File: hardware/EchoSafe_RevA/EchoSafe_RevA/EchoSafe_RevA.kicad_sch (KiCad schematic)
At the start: 27 parts, among them J1 TP4056_Module, J2 Conn_Harness_09, J3 Conn_Harness_09, J4 Conn_Harness_07, J5 Conn_Harness_07, U1 ESP32-S3-WROOM-1-N16R8, U2 MAX98357AETE+T, U3 DRV2605LDGS, U5 TCA9548A, U6 DRV2605LDGS, U7 DRV2605LDGS, U8 DRV2605LDGS

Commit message: Fix JST-SH footprint naming error, verify TP4056 pin spacing
Resolved both gaps flagged at the end of the footprint pass:

- JST-SH harness connector names were an unverified guess using a
  "BM0xB-SRSS-TB" prefix. Fetched the actual files from KiCad's own
  kicad-footprints repo and confirmed the real prefix is "SM0xB-SRSS-TB"
  -- JST_SH_SM09B-SRSS-TB_1x09-1MP_P1.00mm_Horizontal (9 signal + 2
  mounting pads) and JST_SH_SM07B-SRSS-TB_1x07-1MP_P1.00mm_Horizontal
  (7 signal + 2 mounting pads) both verified to exist with correct pad
  counts. Fixed all 8 occurrences across all 5 projects (J2/J3/J4/J5 in
  the central pod, one J1 per module).

- Checked TP4056 module pin spacing against multiple independent
  sources; 2.54mm/0.1" through-hole pitch is standard across common
  module variants, confirming the PinHeader_1x04_P2.54mm_Vertical
  placeholder already assigned. Noted this should still get a quick
  physical check against the actual board, since "HiLetGo TP4056"
  covers slightly different revisions.

Verified across all 5 files: paren balance intact, unique UUIDs.

Co-Authored-By: Claude Sonnet 5 <noreply@anthropic.com>
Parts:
- J2, J3: footprint Connector_JST:JST_SH_BM09B-SRSS-TB_1x09-1MP_P1.00mm_Horizontal -> Connector_JST:JST_SH_SM09B-SRSS-TB_1x09-1MP_P1.00mm_Horizontal
- J4, J5: footprint Connector_JST:JST_SH_BM07B-SRSS-TB_1x07-1MP_P1.00mm_Horizontal -> Connector_JST:JST_SH_SM07B-SRSS-TB_1x07-1MP_P1.00mm_Horizontal
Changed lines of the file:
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@@
 			(effects (font (size 1.27 1.27)) (justify left))
 		)
-		(property "Footprint" "Connector_JST:JST_SH_BM09B-SRSS-TB_1x09-1MP_P1.00mm_Horizontal"
+		(property "Footprint" "Connector_JST:JST_SH_SM09B-SRSS-TB_1x09-1MP_P1.00mm_Horizontal"
 			(at 30 195 0)
 			(effects (font (size 1.27 1.27) (italic yes)) (hide yes))
@@
 			(effects (font (size 1.27 1.27)) (justify left))
 		)
-		(property "Footprint" "Connector_JST:JST_SH_BM09B-SRSS-TB_1x09-1MP_P1.00mm_Horizontal"
+		(property "Footprint" "Connector_JST:JST_SH_SM09B-SRSS-TB_1x09-1MP_P1.00mm_Horizontal"
 			(at 70 195 0)
 			(effects (font (size 1.27 1.27) (italic yes)) (hide yes))
@@
 			(effects (font (size 1.27 1.27)) (justify left))
 		)
-		(property "Footprint" "Connector_JST:JST_SH_BM07B-SRSS-TB_1x07-1MP_P1.00mm_Horizontal"
+		(property "Footprint" "Connector_JST:JST_SH_SM07B-SRSS-TB_1x07-1MP_P1.00mm_Horizontal"
 			(at 110 195 0)
 			(effects (font (size 1.27 1.27) (italic yes)) (hide yes))
@@
 			(effects (font (size 1.27 1.27)) (justify left))
 		)
-		(property "Footprint" "Connector_JST:JST_SH_BM07B-SRSS-TB_1x07-1MP_P1.00mm_Horizontal"
+		(property "Footprint" "Connector_JST:JST_SH_SM07B-SRSS-TB_1x07-1MP_P1.00mm_Horizontal"
 			(at 250 195 0)
 			(effects (font (size 1.27 1.27) (italic yes)) (hide yes))

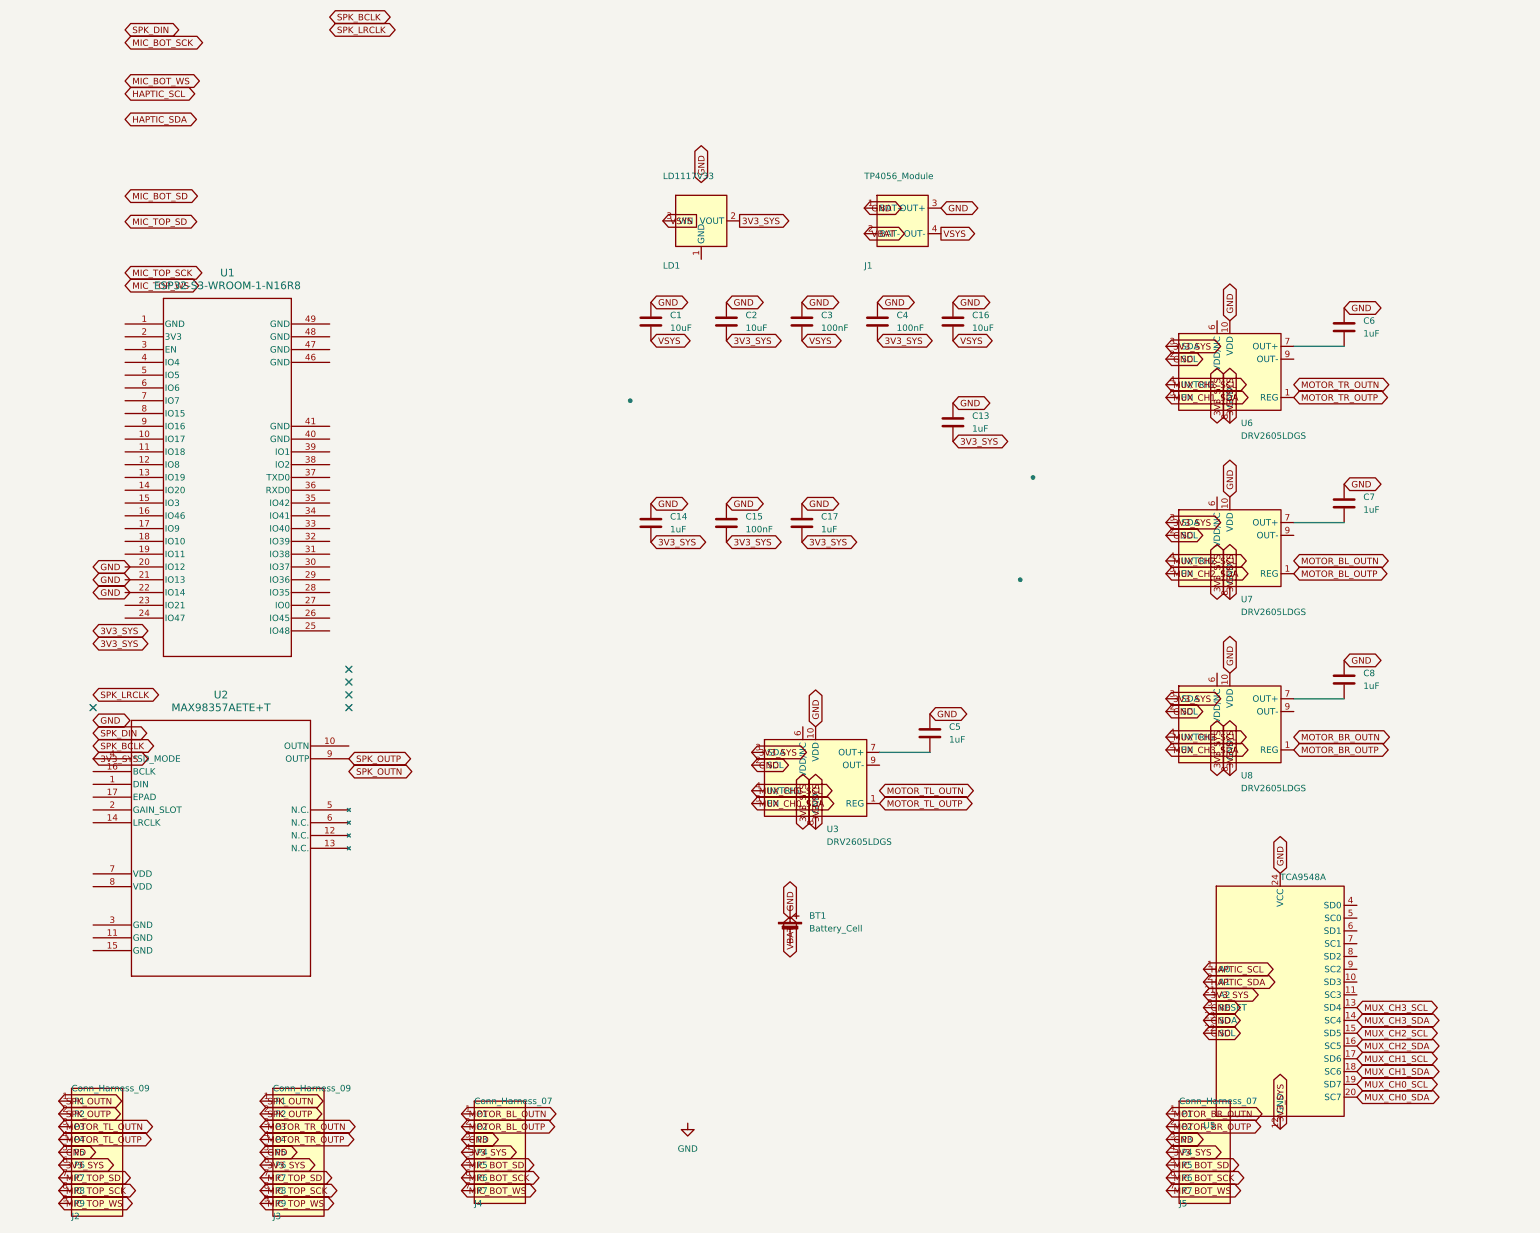
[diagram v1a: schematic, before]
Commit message: Fix session-wide Y-axis coordinate bug, power the ESP32 module
Discovered KiCad is actually installed on this machine and ran real
kicad-cli sch erc against every schematic for the first time, instead of
continuing to rely on text-based invariant checks alone. This surfaced a
fundamental bug affecting every schematic edit made this session:

Every label/wire/no-connect placed with a nonzero local Y pin offset used
placement_y + local_y instead of the correct placement_y - local_y --
KiCad symbol graphics are authored Y-up, the sheet is Y-down, and that
flip applies even at angle=0/no-mirror. The two formulas only agree when
local_y=0, which is why isolated spot-checks earlier in the session
happened to look right.

Fixed via a from-scratch single-pass correction (not sequential in-place
edits -- an earlier attempt at that approach introduced a second bug,
caught before committing: correcting one label could make its new
position collide with a not-yet-corrected label's old position, causing
a later step to move the wrong element). Final approach computes every
correction from an unmodified snapshot and applies them all in one pass
from a fixed baseline.

Verified by ERC before/after, not by the tooling that produced the bug:
- All 4 module projects: 21/21/17/17 raw violations -> 9/9/8/8, all
  expected (spare GPIOs, the already-documented placeholder-connector
  warning, and cross-project "power not driven" since the driving
  component lives in a different project's file).
- Central pod: down to 0 dangling labels, 0 genuinely unconnected pins.
  Remaining ~200 ERC items are exclusively pairwise power-rail type-
  mismatch warnings (expected on any board with this many ICs sharing
  3V3_SYS/GND), cosmetic off-grid warnings, and spare pins.

Also fixed, a genuine gap this same ERC pass surfaced (unrelated to the
Y-axis bug): the ESP32 module's own 3V3/GND/EN pins were never wired to
anything -- every peripheral got connected this session, the MCU's own
supply pins we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
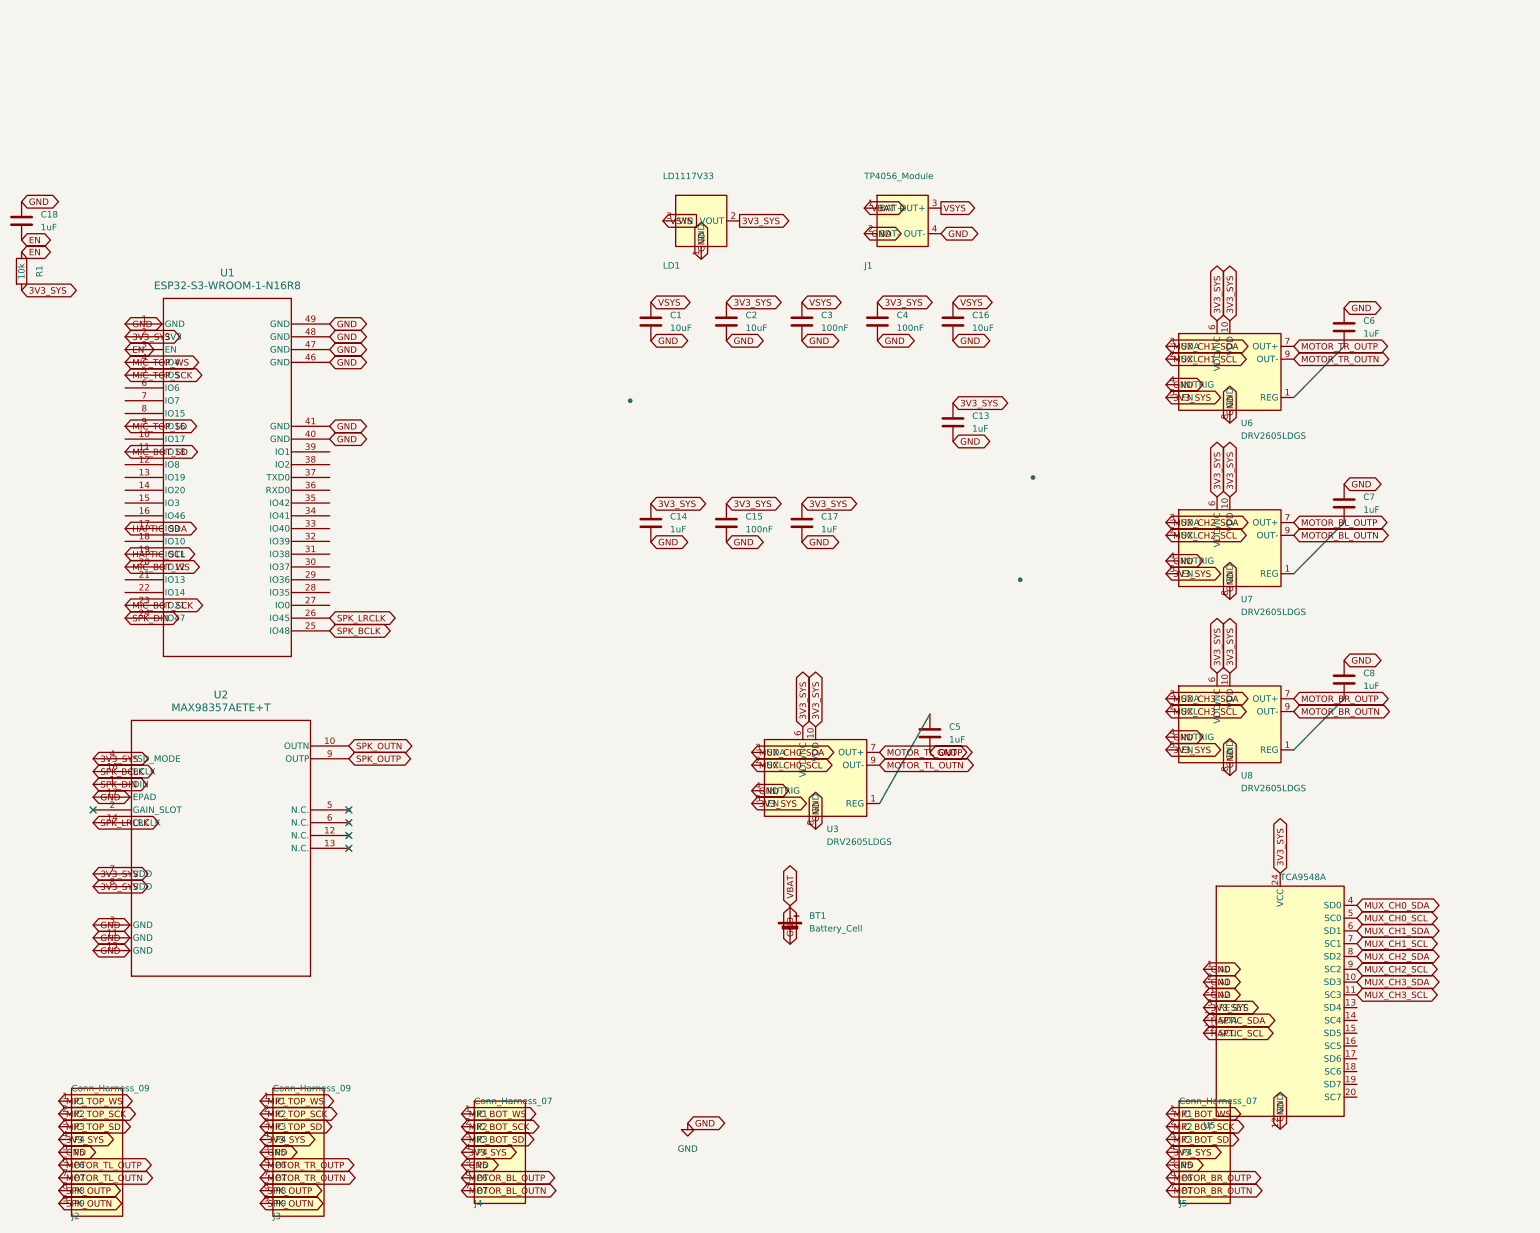
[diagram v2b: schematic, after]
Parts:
- added C18: 1uF, Capacitor_SMD:C_0603_1608Metric, symbol Device:C
- added R1: 10k, Resistor_SMD:R_0603_1608Metric, symbol Device:R
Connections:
- net 3V3_SYS: now also C13.1, C14.1, C15.1, C17.1, C2.1, C4.1, J2.4 (P4), J3.4 (P4), U1.2 (3V3), U2.7 (VDD), U2.8 (VDD), U3.10 (VDD), U3.5 (EN), U3.6 (VDD/NC), U5.24 (VCC), U5.3 (RESET), U6.10 (VDD), U6.5 (EN), U6.6 (VDD/NC), U7.10 (VDD), U7.5 (EN), U7.6 (VDD/NC), U8.10 (VDD), U8.5 (EN), U8.6 (VDD/NC), R1.2; no longer C13.2, C14.2, C15.2, C17.2, C2.2, C4.2, J2.6 (P6), J3.6 (P6), U3.3 (SDA), U3.8 (GND), U5.12 (GND), U5.21 (A2), U6.3 (SDA), U6.8 (GND), U7.3 (SDA), U7.8 (GND), U8.3 (SDA), U8.8 (GND)
- net GND: now also BT1.2 (-), C1.2, C13.2, C14.2, C15.2, C16.2, C17.2, C2.2, C3.2, C4.2, C5.2, J1.2 (BAT-), J1.4 (OUT-), J4.5 (P5), J5.5 (P5), LD1.1 (GND), U1.1 (GND), U1.40 (GND), U1.41 (GND), U1.46 (GND), U1.47 (GND), U1.48 (GND), U1.49 (GND), U2.11 (GND), U2.15 (GND), U2.17 (EPAD), U2.3 (GND), U3.4 (IN/TRIG), U3.8 (GND), U5.1 (A0), U5.12 (GND), U5.2 (A1), U5.21 (A2), U6.4 (IN/TRIG), U6.8 (GND), U7.4 (IN/TRIG), U7.8 (GND), U8.4 (IN/TRIG), U8.8 (GND), C18.1; no longer C1.1, C13.1, C14.1, C15.1, C16.1, C17.1, C2.1, C3.1, C4.1, C5.1, J1.1 (BAT+), J1.3 (OUT+), J4.3 (P3), J5.3 (P3), U3.10 (VDD), U3.2 (SCL), U5.22 (SCL), U5.23 (SDA), U5.24 (VCC), U5.3 (RESET), U6.10 (VDD), U6.2 (SCL), U7.10 (VDD), U7.2 (SCL), U8.10 (VDD), U8.2 (SCL)
- net HAPTIC_SCL: now also U1.19 (IO11), U5.22 (SCL); no longer U5.1 (A0)
- net HAPTIC_SDA: now also U1.17 (IO9), U5.23 (SDA); no longer U5.2 (A1)
- net MIC_BOT_SCK: now also J4.2 (P2), J5.2 (P2), U1.23 (IO21); no longer J4.6 (P6), J5.6 (P6)
- net MIC_BOT_SD: now also J4.3 (P3), J5.3 (P3), U1.11 (IO18); no longer J4.5 (P5), J5.5 (P5)
- net MIC_BOT_WS: now also J4.1 (P1), J5.1 (P1), U1.20 (IO12); no longer J4.7 (P7), J5.7 (P7)
- net MIC_TOP_SCK: now also J2.2 (P2), J3.2 (P2), U1.5 (IO5); no longer J2.8 (P8), J3.8 (P8)
- net MIC_TOP_SD: now also J2.3 (P3), J3.3 (P3), U1.9 (IO16); no longer J2.7 (P7), J3.7 (P7)
- net MIC_TOP_WS: now also J2.1 (P1), J3.1 (P1), U1.4 (IO4); no longer J2.9 (P9), J3.9 (P9)
- net MOTOR_BL_OUTN: now also J4.7 (P7), U7.9 (OUT-); no longer J4.1 (P1)
- net MOTOR_BL_OUTP: now also J4.6 (P6), U7.7 (OUT+); no longer J4.2 (P2), U7.1 (REG)
- net MOTOR_BR_OUTN: now also J5.7 (P7), U8.9 (OUT-); no longer J5.1 (P1)
- net MOTOR_BR_OUTP: now also J5.6 (P6), U8.7 (OUT+); no longer J5.2 (P2), U8.1 (REG)
- net MOTOR_TL_OUTN: now also J2.7 (P7), U3.9 (OUT-); no longer J2.3 (P3)
- net MOTOR_TL_OUTP: now also J2.6 (P6), U3.7 (OUT+); no longer J2.4 (P4), U3.1 (REG)
- net MOTOR_TR_OUTN: now also J3.7 (P7), U6.9 (OUT-); no longer J3.3 (P3)
- net MOTOR_TR_OUTP: now also J3.6 (P6), U6.7 (OUT+); no longer J3.4 (P4), U6.1 (REG)
- net MUX_CH0_SCL: now also U3.2 (SCL), U5.5 (SC0); no longer U3.4 (IN/TRIG), U5.19 (SD7)
- net MUX_CH0_SDA: now also U3.3 (SDA), U5.4 (SD0); no longer U3.5 (EN), U5.20 (SC7)
- net MUX_CH1_SCL: now also U5.7 (SC1), U6.2 (SCL); no longer U5.17 (SD6), U6.4 (IN/TRIG)
- net MUX_CH1_SDA: now also U5.6 (SD1), U6.3 (SDA); no longer U5.18 (SC6), U6.5 (EN)
- net MUX_CH2_SCL: now also U5.9 (SC2), U7.2 (SCL); no longer U5.15 (SD5), U7.4 (IN/TRIG)
- net MUX_CH2_SDA: now also U5.8 (SD2), U7.3 (SDA); no longer U5.16 (SC5), U7.5 (EN)
- net MUX_CH3_SCL: now also U5.11 (SC3), U8.2 (SCL); no longer U5.13 (SD4), U8.4 (IN/TRIG)
- net MUX_CH3_SDA: now also U5.10 (SD3), U8.3 (SDA); no longer U5.14 (SC4), U8.5 (EN)
- net SPK_BCLK: now also U1.25 (IO48), U2.16 (BCLK)
- net SPK_DIN: now also U1.24 (IO47), U2.1 (DIN)
- net SPK_LRCLK: now also U1.26 (IO45), U2.14 (LRCLK)
- net SPK_OUTN: now also J2.9 (P9), J3.9 (P9), U2.10 (OUTN); no longer J2.1 (P1), J3.1 (P1)
- net SPK_OUTP: now also J2.8 (P8), J3.8 (P8); no longer J2.2 (P2), J3.2 (P2)
- net VBAT: now also BT1.1 (+), J1.1 (BAT+); no longer J1.2 (BAT-)
- net VSYS: now also C1.1, C16.1, C3.1, J1.3 (OUT+); no longer C1.2, C16.2, C3.2, J1.4 (OUT-)
- net at C8.2: now also U8.1 (REG); no longer U8.7 (OUT+)
- net at C6.2: now also U6.1 (REG); no longer U6.7 (OUT+)
- net at C7.2: now also U7.1 (REG); no longer U7.7 (OUT+)
- net EN: now reaches U1.3 (EN)
- net EN: now also C18.2, R1.1
- new net: C5.1, U3.1 (REG)

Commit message: Complete PCB layout for all 5 boards, all DRC-clean
All 4 earpiece module boards and the central pod are now placed, fully
routed, and verified at 0 DRC violations / 0 unconnected pads via
kicad-cli. The central pod (the largest/densest board) was routed with
FreeRouting (Specctra DSN export/import) after hand-scripted routing
failed to converge; the last few gaps FreeRouting left were fixed by
hand with precise pad/via clearance geometry. Documented the full
approach and key lessons in CLAUDE.md for future reference.

Co-Authored-By: Claude Sonnet 5 <noreply@anthropic.com>
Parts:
- BT1: footprint Connector_JST:JST_PH_S2B_PH_K_1x02_P2.00mm_Horizontal -> Connector_JST:JST_PH_S2B-PH-K_1x02_P2.00mm_Horizontal
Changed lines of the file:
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@@
 			)
 		)
-		(property "Footprint" "Connector_JST:JST_PH_S2B_PH_K_1x02_P2.00mm_Horizontal"
+		(property "Footprint" "Connector_JST:JST_PH_S2B-PH-K_1x02_P2.00mm_Horizontal"
 			(at 167.64 149.606 90)
 			(effects

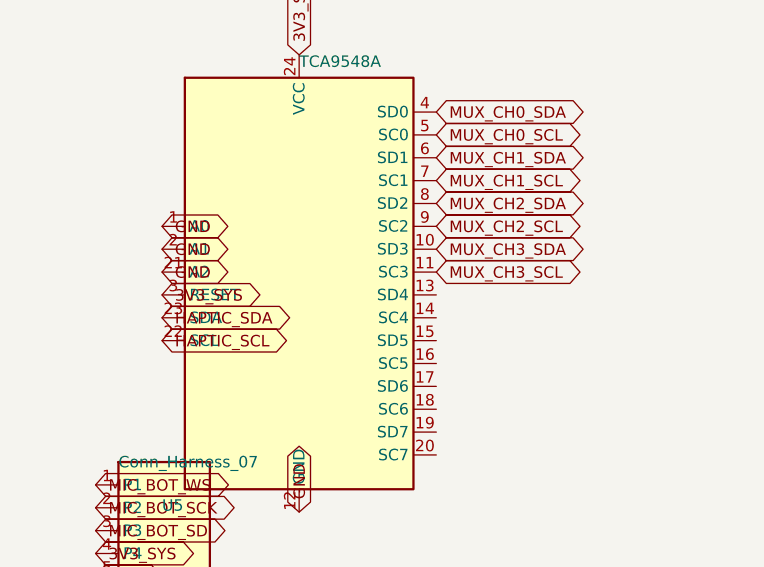
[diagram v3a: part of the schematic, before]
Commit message: Replace TCA9548A RESET direct tie with proper pull-up resistor
TI's TCA9548A datasheet specifies RESET should connect to VCC through
a pull-up resistor when unused, not a direct tie. Added R2 (10kΩ,
matching R1's EN pull-up convention) between RESET and 3V3_SYS.
Verified with kicad-cli sch erc: same violation count/categories as
before (211 -> 210), no new unconnected pins.

Co-Authored-By: Claude Sonnet 5 <noreply@anthropic.com>
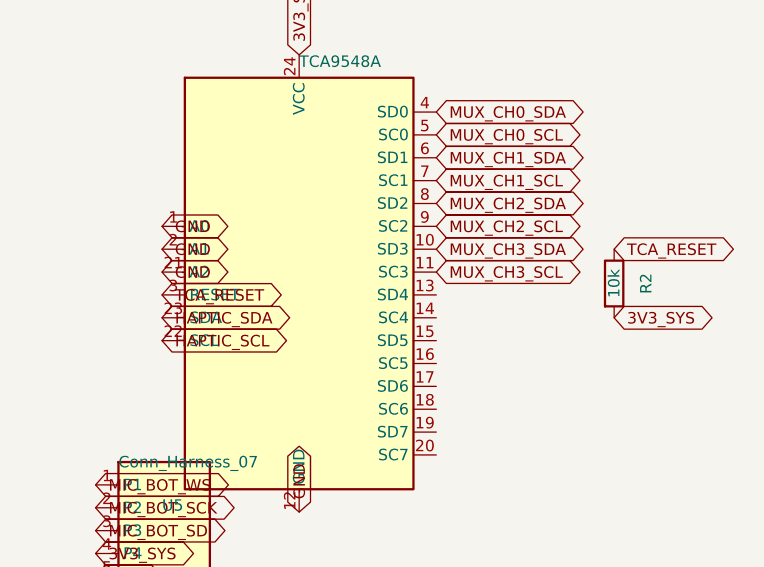
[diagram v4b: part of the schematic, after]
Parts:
- added R2: 10k, Resistor_SMD:R_0603_1608Metric, symbol Device:R
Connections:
- net 3V3_SYS: now also R2.2; no longer U5.3 (RESET)
- new net TCA_RESET: R2.1, U5.3 (RESET)
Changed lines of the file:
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@@
 		)
 	)
-	(global_label "3V3_SYS"
+	(global_label "TCA_RESET"
 		(shape bidirectional)
 		(at 249.76 166.27 0)
@@
 			(effects
 				(font
+					(size 1.27 1.27)
+				)
+				(justify left)
+				(hide yes)
+			)
+		)
+	)
+	(symbol
+		(lib_id "Device:R")
+		(at 300 165 0)
+		(unit 1)
+		(exclude_from_sim no)
+		(in_bom yes)
+		(on_board yes)
+		(dnp no)
+		(fields_autoplaced yes)
+		(property "Reference" "R2"
+			(at 303.556 165 90)
+			(effects (font (size 1.27 1.27)))
+		)
+		(property "Value" "10k"
+			(at 300 165 90)
+			(effects (font (size 1.27 1.27)))
+		)
+		(property "Footprint" "Resistor_SMD:R_0603_1608Metric"
+			(at 296.889 165 90)
+			(effects (font (size 1.27 1.27) (italic yes)) (hide yes))
+		)
+		(property "Datasheet" "~"
+			(at 300 165 0)
+			(effects (font (size 1.27 1.27)) (hide yes))
+		)
+		(property "Description" "TCA9548A RESET pull-up (datasheet: 'Connect to VCC ... through a pull-up resistor, if not used'), 10k matching the same convention as R1's EN pull-up"
+			(at 300 165 0)
+			(effects (font (size 1.27 1.27)) (hide yes))
+		)
+		(pin "1"
+		)
+		(pin "2"
+		)
+		(instances
+			(project "EchoSafe_RevA"
+				(path "/bdb2d0da-eb9b-4e92-86e3-ab6f2cfb466f"
+					(reference "R2")
+					(unit 1)
+				)
+			)
+		)
+	)
+	(global_label "TCA_RESET"
+		(shape bidirectional)
+		(at 300 161.19 0)
+		(fields_autoplaced yes)
+		(effects
+			(font
+				(size 1.27 1.27)
+			)
+			(justify left)
+		)
+		(property "Intersheetrefs" "${INTERSHEET_REFS}"
+			(at 305 161.19 0)
+			(effects
+				(font
+					(size 1.27 1.27)
+				)
+				(justify left)
+				(hide yes)
+			)
+		)
+	)
+	(global_label "3V3_SYS"
+		(shape bidirectional)
+		(at 300 168.81 0)
+		(fields_autoplaced yes)
+		(effects
+			(font
+				(size 1.27 1.27)
+			)
+			(justify left)
+		)
+		(property "Intersheetrefs" "${INTERSHEET_REFS}"
+			(at 305 168.81 0)
+			(effects
+				(font
